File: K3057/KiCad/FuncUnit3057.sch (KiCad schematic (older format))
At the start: 26 parts, among them J11 PAD, J12 PAD, J14 PAD, J16 PAD, J18 PAD, J19 PAD, Q11 SSM6N7002BFE, Q12 SSM6N7002BFE, Q13 SSM6N7002BFE, Q14 SSM6N7002BFE, Q15 SSM3K7002BFU

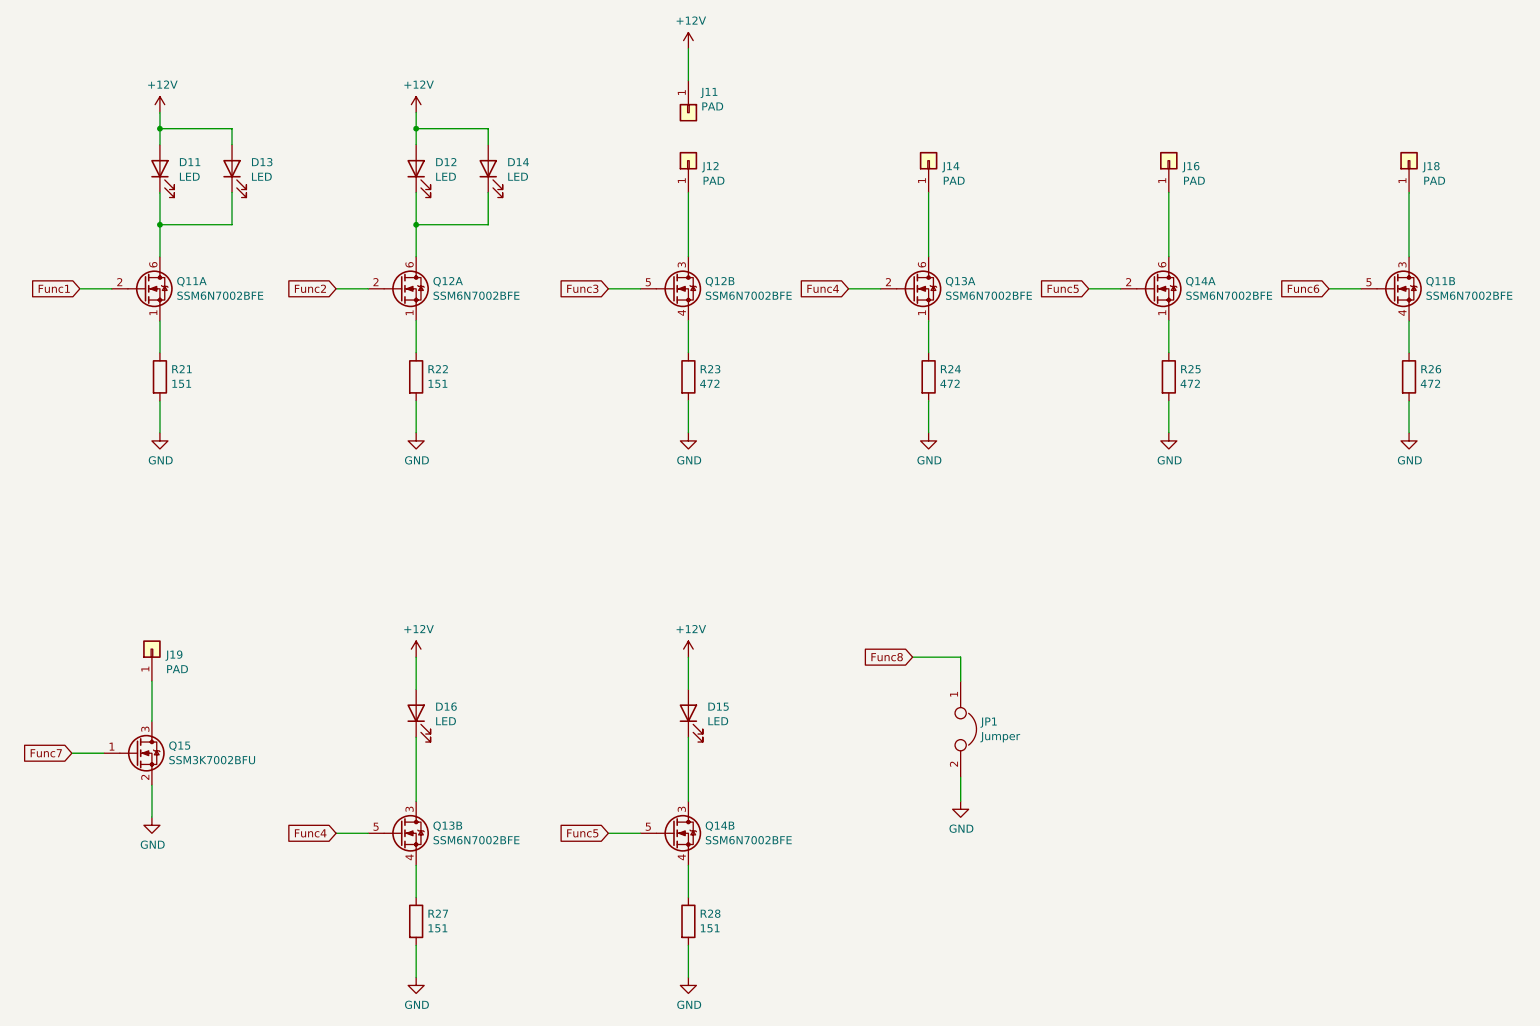
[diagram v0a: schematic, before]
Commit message: 回路の問題点を修正 (K3066: Rev3 / それ以外: Rev2)
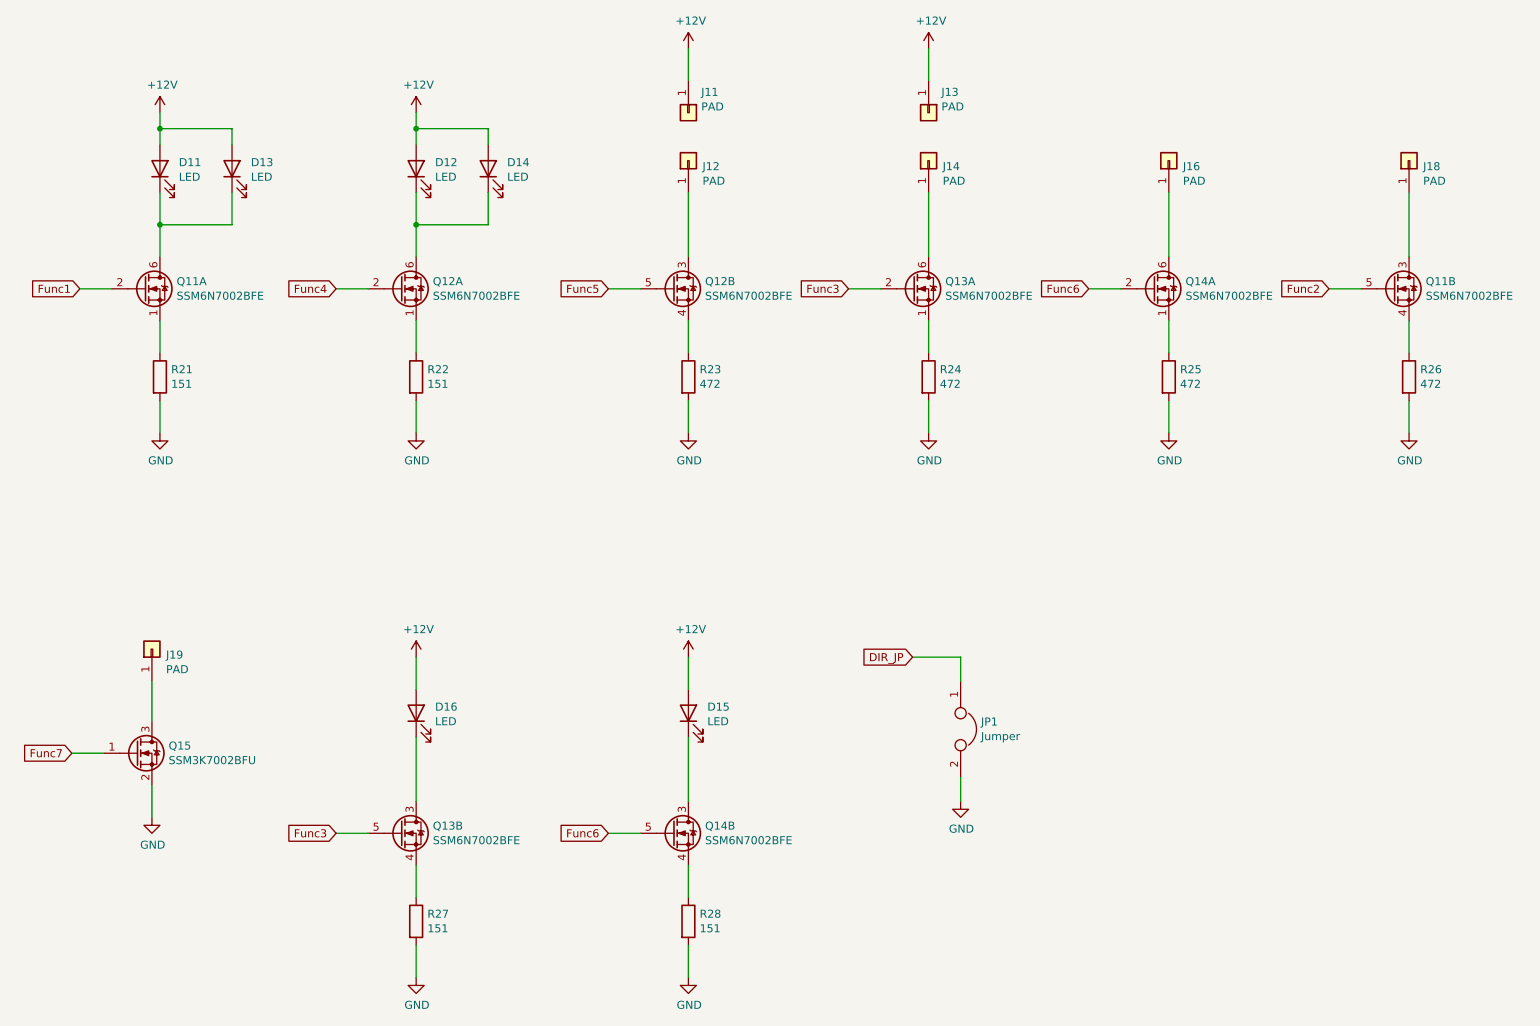
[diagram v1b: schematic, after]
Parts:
- added J13: PAD, footprint:PAD_1.0x1.8_SMD, symbol Connector_Generic:Conn_01x01
- J19: footprint footprint:PAD_0.6x1.0_SMD -> footprint:PAD_1.0x1.4_SMD
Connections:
- net +12V: now also J13.1 (Pin_1)
- net Func2: now also Q11.5 (G); no longer Q12.2 (G)
- net Func3: now also Q13.2 (G), Q13.5 (G); no longer Q12.5 (G)
- net Func4: now also Q12.2 (G); no longer Q13.2 (G), Q13.5 (G)
- net Func5: now also Q12.5 (G); no longer Q14.2 (G), Q14.5 (G)
- net Func6: now also Q14.2 (G), Q14.5 (G); no longer Q11.5 (G)
- net Func8 renamed DIR_JP
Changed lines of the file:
@@
 Func1
 Text GLabel 4800 2600 0    50   Input ~ 0
-Func3
+Func5
 Wire Wire Line
 	5000 2600 4800 2600
@@
 	6800 3000 6800 2800
 Text GLabel 6300 2600 0    50   Input ~ 0
-Func4
+Func3
 Wire Wire Line
 	6500 2600 6300 2600
@@
 	8300 3000 8300 2800
 Text GLabel 7800 2600 0    50   Input ~ 0
-Func5
+Func6
 Wire Wire Line
 	8000 2600 7800 2600
@@
 	9800 3000 9800 2800
 Text GLabel 9300 2600 0    50   Input ~ 0
-Func6
+Func2
 Wire Wire Line
 	9500 2600 9300 2600
@@
 	3600 3300 3600 3500
 Text GLabel 3100 2600 0    50   Input ~ 0
-Func2
+Func4
 Wire Wire Line
 	3300 2600 3100 2600
@@
 $EndComp
 Text GLabel 4800 6000 0    50   Input ~ 0
-Func5
+Func6
 Wire Wire Line
 	5000 6000 4800 6000
@@
 $EndComp
 Text GLabel 6700 4900 0    50   Input ~ 0
-Func8
+DIR_JP
 Wire Wire Line
 	6700 4900 7000 4900
@@
 F 0 "J19" V 1914 4762 50  0000 R CNN
 F 1 "PAD" V 1823 4762 50  0000 R CNN
-F 2 "footprint:PAD_0.6x1.0_SMD" H 1950 4850 50  0001 C CNN
+F 2 "footprint:PAD_1.0x1.4_SMD" H 1950 4850 50  0001 C CNN
 F 3 "~" H 1950 4850 50  0001 C CNN
 	1    1950 4850
@@
 	1    0    0    -1
 $EndComp
-Text GLabel 3100 6000 0    50   Input ~ 0
-Func4
 Wire Wire Line
 	3300 6000 3100 6000
@@
 $EndComp
 $Comp
-L power:GND #PWR?
+L power:GND #PWR0137
 U 1 1 6048E65A
 P 3600 6900
-F 0 "#PWR?" H 3600 6650 50  0001 C CNN
+F 0 "#PWR0137" H 3600 6650 50  0001 C CNN
 F 1 "GND" H 3605 6727 50  0000 C CNN
 F 2 "" H 3600 6900 50  0001 C CNN
@@
 $EndComp
 $Comp
-L power:+12V #PWR?
+L power:+12V #PWR0138
 U 1 1 6048E670
 P 3600 4900
-F 0 "#PWR?" H 3600 4750 50  0001 C CNN
+F 0 "#PWR0138" H 3600 4750 50  0001 C CNN
 F 1 "+12V" H 3615 5073 50  0000 C CNN
 F 2 "" H 3600 4900 50  0001 C CNN
@@
 Wire Wire Line
 	3600 5400 3600 5800
+$Comp
+L Connector_Generic:Conn_01x01 J13
+U 1 1 6093B9B8
+P 6800 1500
+F 0 "J13" V 6672 1580 50  0000 L CNN
+F 1 "PAD" V 6763 1580 50  0000 L CNN
+F 2 "footprint:PAD_1.0x1.8_SMD" H 6800 1500 50  0001 C CNN
+F 3 "~" H 6800 1500 50  0001 C CNN
+	1    6800 1500
+	0    1    1    0
+$EndComp
+Wire Wire Line
+	6800 1300 6800 1100
+$Comp
+L power:+12V #PWR0139
+U 1 1 6093CF27
+P 6800 1100
+F 0 "#PWR0139" H 6800 950 50  0001 C CNN
+F 1 "+12V" H 6815 1273 50  0000 C CNN
+F 2 "" H 6800 1100 50  0001 C CNN
+F 3 "" H 6800 1100 50  0001 C CNN
+	1    6800 1100
+	1    0    0    -1
+$EndComp
+Text GLabel 3100 6000 0    50   Input ~ 0
+Func3
 $EndSCHEMATC

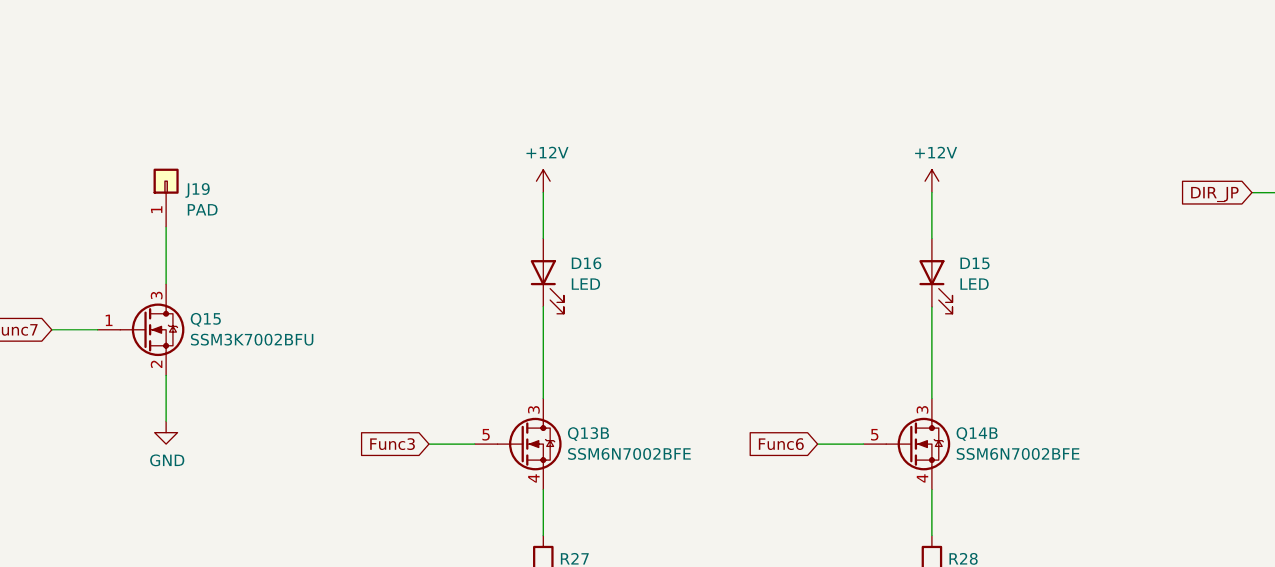
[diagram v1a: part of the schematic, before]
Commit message: (K3057RA) 表面のLEDパッドを増設
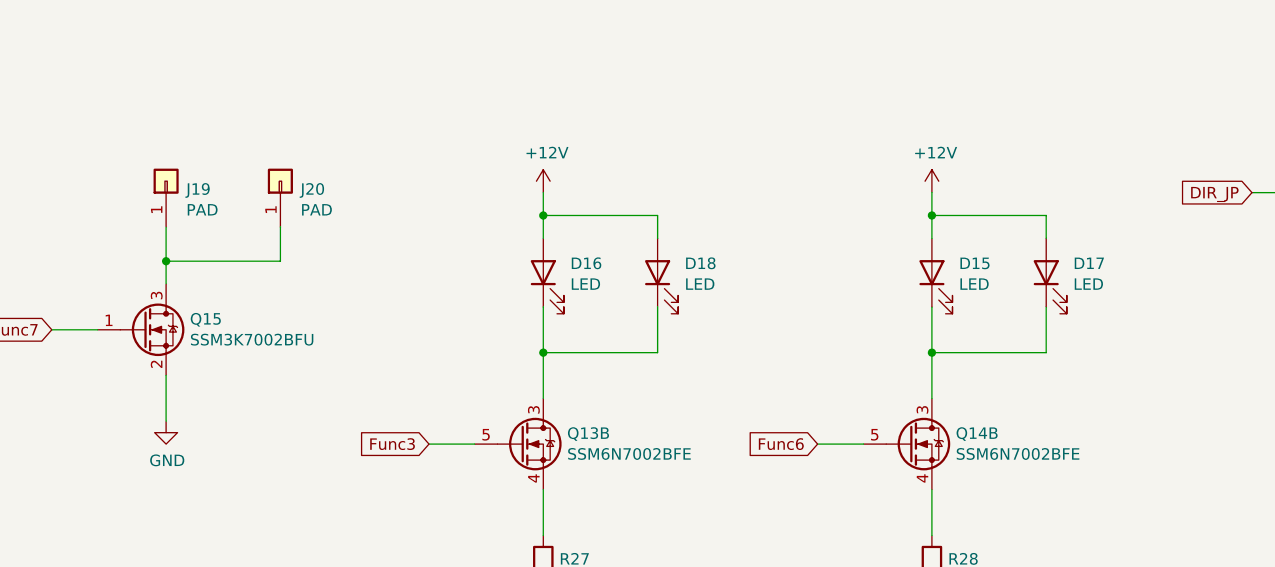
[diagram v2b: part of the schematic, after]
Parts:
- added D17, D18: LED, footprint:LED_1224_1005_SIDE_BIG2, symbol Device:LED
- added J20: PAD, footprint:PAD_0.5x1.2_SMD, symbol Connector_Generic:Conn_01x01
- D11, D12, D13, D14, D15, D16: footprint footprint:LED_1224_1005_SIDE -> footprint:LED_1224_1005_SIDE_BIG2
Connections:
- net +12V: now also D17.2 (A), D18.2 (A)
- net at D16.1 (K), Q13.3 (D): now also D18.1 (K)
- net at J19.1 (Pin_1), Q15.3 (D): now also J20.1 (Pin_1)
- net at D15.1 (K), Q14.3 (D): now also D17.1 (K)
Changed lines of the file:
@@
 F 0 "D11" V 2039 1732 50  0000 R CNN
 F 1 "LED" V 1948 1732 50  0000 R CNN
-F 2 "footprint:LED_1224_1005_SIDE" H 2000 1850 50  0001 C CNN
+F 2 "footprint:LED_1224_1005_SIDE_BIG2" H 2000 1850 50  0001 C CNN
 F 3 "~" H 2000 1850 50  0001 C CNN
 	1    2000 1850
@@
 F 0 "D12" V 3639 1732 50  0000 R CNN
 F 1 "LED" V 3548 1732 50  0000 R CNN
-F 2 "footprint:LED_1224_1005_SIDE" H 3600 1850 50  0001 C CNN
+F 2 "footprint:LED_1224_1005_SIDE_BIG2" H 3600 1850 50  0001 C CNN
 F 3 "~" H 3600 1850 50  0001 C CNN
 	1    3600 1850
@@
 F 0 "D15" V 5339 5132 50  0000 R CNN
 F 1 "LED" V 5248 5132 50  0000 R CNN
-F 2 "footprint:LED_1224_1005_SIDE" H 5300 5250 50  0001 C CNN
+F 2 "footprint:LED_1224_1005_SIDE_BIG2" H 5300 5250 50  0001 C CNN
 F 3 "~" H 5300 5250 50  0001 C CNN
 	1    5300 5250
@@
 $EndComp
 Wire Wire Line
-	5300 5100 5300 4900
-Wire Wire Line
-	5300 5400 5300 5800
+	5300 5100 5300 5000
+Wire Wire Line
+	5300 5400 5300 5600
 $Comp
 L Device:Jumper JP1
@@
 F 0 "D14" V 4089 1732 50  0000 R CNN
 F 1 "LED" V 3998 1732 50  0000 R CNN
-F 2 "footprint:LED_1224_1005_SIDE" H 4050 1850 50  0001 C CNN
+F 2 "footprint:LED_1224_1005_SIDE_BIG2" H 4050 1850 50  0001 C CNN
 F 3 "~" H 4050 1850 50  0001 C CNN
 	1    4050 1850
@@
 F 0 "D13" V 2489 1732 50  0000 R CNN
 F 1 "LED" V 2398 1732 50  0000 R CNN
-F 2 "footprint:LED_1224_1005_SIDE" H 2450 1850 50  0001 C CNN
+F 2 "footprint:LED_1224_1005_SIDE_BIG2" H 2450 1850 50  0001 C CNN
 F 3 "~" H 2450 1850 50  0001 C CNN
 	1    2450 1850
@@
 	2000 2200 2000 2400
 Wire Wire Line
-	1950 5050 1950 5300
+	1950 5050 1950 5200
 $Comp
 L Connector_Generic:Conn_01x01 J19
@@
 F 0 "D16" V 3639 5132 50  0000 R CNN
 F 1 "LED" V 3548 5132 50  0000 R CNN
-F 2 "footprint:LED_1224_1005_SIDE" H 3600 5250 50  0001 C CNN
+F 2 "footprint:LED_1224_1005_SIDE_BIG2" H 3600 5250 50  0001 C CNN
 F 3 "~" H 3600 5250 50  0001 C CNN
 	1    3600 5250
@@
 $EndComp
 Wire Wire Line
-	3600 5100 3600 4900
-Wire Wire Line
-	3600 5400 3600 5800
+	3600 5100 3600 5000
+Wire Wire Line
+	3600 5400 3600 5600
 $Comp
 L Connector_Generic:Conn_01x01 J13
@@
 Text GLabel 3100 6000 0    50   Input ~ 0
 Func3
+$Comp
+L Device:LED D17
+U 1 1 61DCBAEC
+P 5800 5250
+F 0 "D17" V 5839 5132 50  0000 R CNN
+F 1 "LED" V 5748 5132 50  0000 R CNN
+F 2 "footprint:LED_1224_1005_SIDE_BIG2" H 5800 5250 50  0001 C CNN
+F 3 "~" H 5800 5250 50  0001 C CNN
+	1    5800 5250
+	0    -1   -1   0
+$EndComp
+Wire Wire Line
+	5300 5000 5800 5000
+Wire Wire Line
+	5800 5000 5800 5100
+Connection ~ 5300 5000
+Wire Wire Line
+	5300 5000 5300 4900
+Wire Wire Line
+	5300 5600 5800 5600
+Wire Wire Line
+	5800 5600 5800 5400
+Connection ~ 5300 5600
+Wire Wire Line
+	5300 5600 5300 5800
+$Comp
+L Device:LED D18
+U 1 1 61DCF3F4
+P 4100 5250
+F 0 "D18" V 4139 5132 50  0000 R CNN
+F 1 "LED" V 4048 5132 50  0000 R CNN
+F 2 "footprint:LED_1224_1005_SIDE_BIG2" H 4100 5250 50  0001 C CNN
+F 3 "~" H 4100 5250 50  0001 C CNN
+	1    4100 5250
+	0    -1   -1   0
+$EndComp
+Wire Wire Line
+	3600 5000 4100 5000
+Wire Wire Line
+	4100 5000 4100 5100
+Connection ~ 3600 5000
+Wire Wire Line
+	3600 5000 3600 4900
+Wire Wire Line
+	3600 5600 4100 5600
+Wire Wire Line
+	4100 5600 4100 5400
+Connection ~ 3600 5600
+Wire Wire Line
+	3600 5600 3600 5800
+$Comp
+L Connector_Generic:Conn_01x01 J20
+U 1 1 61DD5704
+P 2450 4850
+F 0 "J20" V 2414 4762 50  0000 R CNN
+F 1 "PAD" V 2323 4762 50  0000 R CNN
+F 2 "footprint:PAD_0.5x1.2_SMD" H 2450 4850 50  0001 C CNN
+F 3 "~" H 2450 4850 50  0001 C CNN
+	1    2450 4850
+	0    -1   -1   0
+$EndComp
+Wire Wire Line
+	1950 5200 2450 5200
+Wire Wire Line
+	2450 5200 2450 5050
+Connection ~ 1950 5200
+Wire Wire Line
+	1950 5200 1950 5300
 $EndSCHEMATC
